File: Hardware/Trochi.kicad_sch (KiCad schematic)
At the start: 54 parts, among them IC1 ICM-42688-P, J1 JST-SH, J2 JST-SH, J3 JST PH, J4 JST-SH, J5 JST-SH, J6 JST_SH, Q1 AO3401A, Q2 AO3400A, Q3 AO3400A, Q4 AO3400A, Q5 AO3400A, Q6 AO3400A, SW1 SW_SPDT, U1 ME6211C33M5, U3 YX-SMD5020

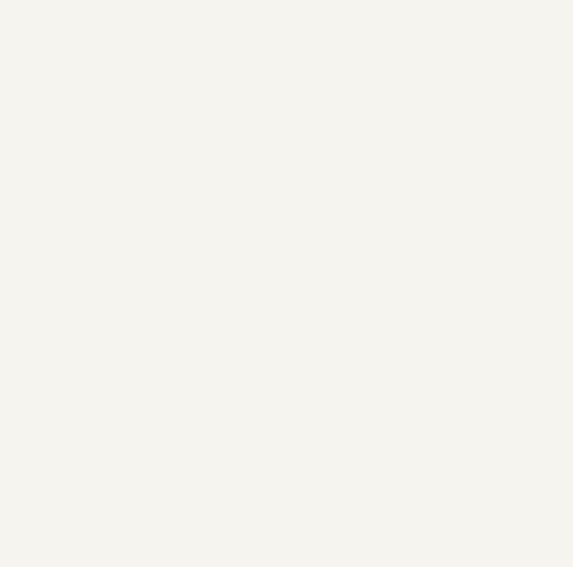
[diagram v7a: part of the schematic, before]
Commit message: feat: start bottom layer routing on PCB
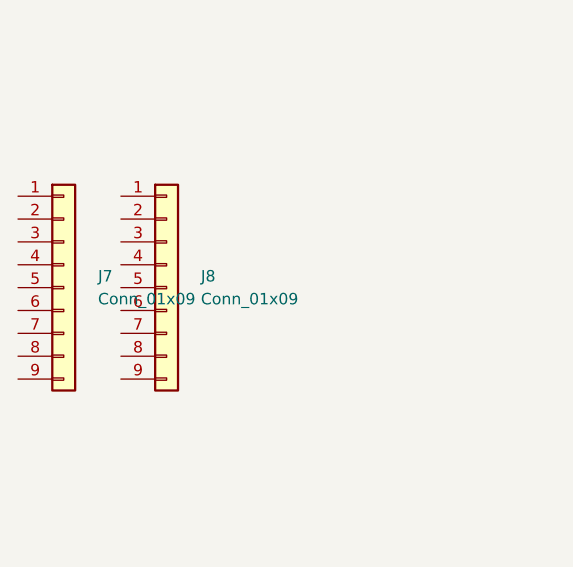
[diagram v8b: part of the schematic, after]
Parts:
- added J7, J8: Conn_01x09, Connector_PinHeader_2.54mm:PinHeader_1x09_P2.54mm_Vertical, symbol Connector_Generic:Conn_01x09
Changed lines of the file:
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@@
+	)
+	(symbol
+		(lib_id "Connector_Generic:Conn_01x09")
+		(at -45.72 44.45 0)
+		(unit 1)
+		(body_style 1)
+		(exclude_from_sim no)
+		(in_bom yes)
+		(on_board yes)
+		(in_pos_files yes)
+		(dnp no)
+		(fields_autoplaced yes)
+		(property "Reference" "J8"
+			(at -41.91 43.1799 0)
+			(show_name no)
+			(do_not_autoplace no)
+			(effects
+				(font
+					(size 1.27 1.27)
+				)
+				(justify left)
+			)
+		)
+		(property "Value" "Conn_01x09"
+			(at -41.91 45.7199 0)
+			(show_name no)
+			(do_not_autoplace no)
+			(effects
+				(font
+					(size 1.27 1.27)
+				)
+				(justify left)
+			)
+		)
+		(property "Footprint" "Connector_PinHeader_2.54mm:PinHeader_1x09_P2.54mm_Vertical"
+			(at -45.72 44.45 0)
+			(hide yes)
+			(show_name no)
+			(do_not_autoplace no)
+			(effects
+				(font
+					(size 1.27 1.27)
+				)
+			)
+		)
+		(property "Datasheet" ""
+			(at -45.72 44.45 0)
+			(hide yes)
+			(show_name no)
+			(do_not_autoplace no)
+			(effects
+				(font
+					(size 1.27 1.27)
+				)
+			)
+		)
+		(property "Description" "Generic connector, single row, 01x09, script generated (kicad-library-utils/schlib/autogen/connector/)"
+			(at -45.72 44.45 0)
+			(hide yes)
+			(show_name no)
+			(do_not_autoplace no)
+			(effects
+				(font
+					(size 1.27 1.27)
+				)
+			)
+		)
+		(pin "5"
+		)
+		(pin "8"
+		)
+		(pin "1"
+		)
+		(pin "2"
+		)
+		(pin "6"
+		)
+		(pin "3"
+		)
+		(pin "7"
+		)
+		(pin "4"
+		)
+		(pin "9"
+		)
+		(instances
+			(project "Trochi"
+				(path "/a5119cab-c33d-484e-b542-18705d0dc8d0"
+					(reference "J8")
+					(unit 1)
+				)
+			)
+		)
 	)
 	(symbol
@@
 					(unit 1)
 				)
+			)
+		)
+	)
+	(symbol
+		(lib_id "Connector_Generic:Conn_01x09")
+		(at -57.15 44.45 0)
+		(unit 1)
+		(body_style 1)
+		(exclude_from_sim no)
+		(in_bom yes)
+		(on_board yes)
+		(in_pos_files yes)
+		(dnp no)
+		(fields_autoplaced yes)
+		(property "Reference" "J7"
+			(at -53.34 43.1799 0)
+			(show_name no)
+			(do_not_autoplace no)
+			(effects
+				(font
+					(size 1.27 1.27)
+				)
+				(justify left)
+			)
+		)
+		(property "Value" "Conn_01x09"
+			(at -53.34 45.7199 0)
+			(show_name no)
+			(do_not_autoplace no)
+			(effects
+				(font
+					(size 1.27 1.27)
+				)
+				(justify left)
+			)
+		)
+		(property "Footprint" "Connector_PinHeader_2.54mm:PinHeader_1x09_P2.54mm_Vertical"
+			(at -57.15 44.45 0)
+			(hide yes)
+			(show_name no)
+			(do_not_autoplace no)
+			(effects
+				(font
+					(size 1.27 1.27)
+				)
+			)
+		)
+		(property "Datasheet" ""
+			(at -57.15 44.45 0)
+			(hide yes)
+			(show_name no)
+			(do_not_autoplace no)
+			(effects
+				(font
+					(size 1.27 1.27)
+				)
+			)
+		)
+		(property "Description" "Generic connector, single row, 01x09, script generated (kicad-library-utils/schlib/autogen/connector/)"
+			(at -57.15 44.45 0)
+			(hide yes)
+			(show_name no)
+			(do_not_autoplace no)
+			(effects
+				(font
+					(size 1.27 1.27)
+				)
+			)
+		)
+		(pin "5"
+		)
+		(pin "8"
+		)
+		(pin "1"
+		)
+		(pin "2"
+		)
+		(pin "6"
+		)
+		(pin "3"
+		)
+		(pin "7"
+		)
+		(pin "4"
+		)
+		(pin "9"
+		)
+		(instances
+			(project "Trochi"
+				(path "/a5119cab-c33d-484e-b542-18705d0dc8d0"
+					(reference "J7")
+					(unit 1)
+				)
